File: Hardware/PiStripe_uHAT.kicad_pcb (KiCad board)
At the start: 2 copper layers, 65 x 30 mm, 43 parts, among them J1 +12V, J2 LED, J3 IRRX, J4 RPi_GPIO, Q1 DMG2305UX-13, Q2 IRF8721PBF-1, Q3 IRF8721PBF-1, Q4 IRF8721PBF-1, U1 TPS54202, U2 DMMT5401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

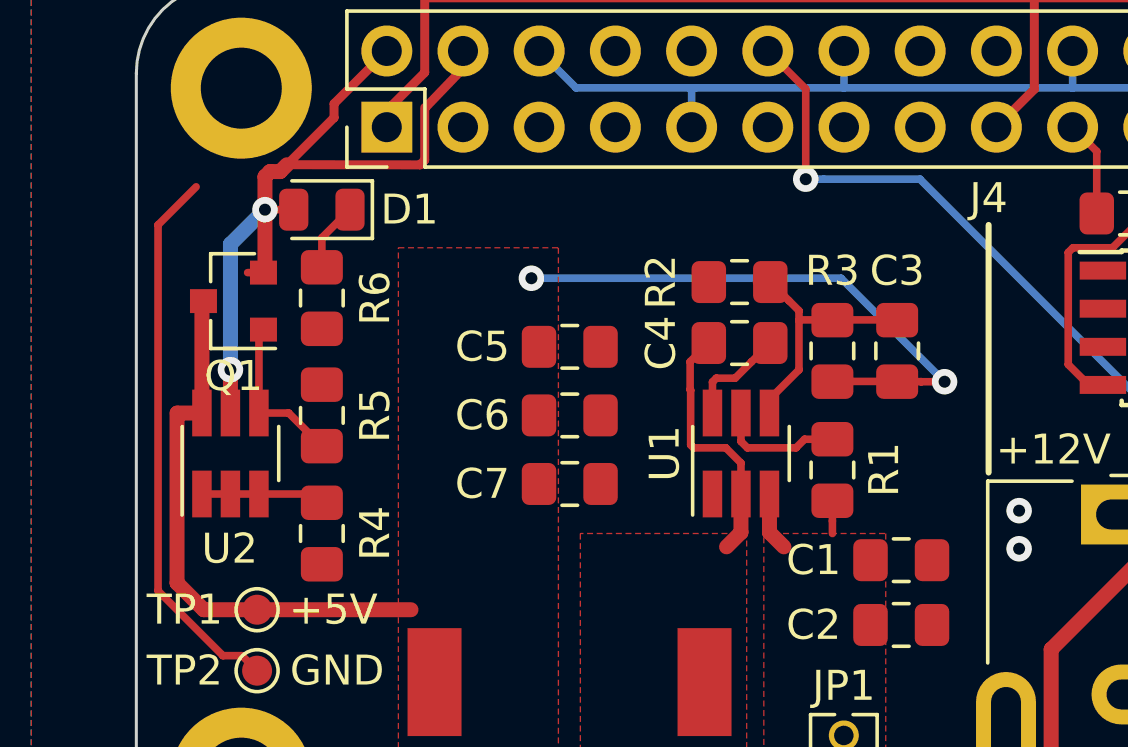
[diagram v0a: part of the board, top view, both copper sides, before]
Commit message: PCB: Add one more guide line, move C5-C7 a bit
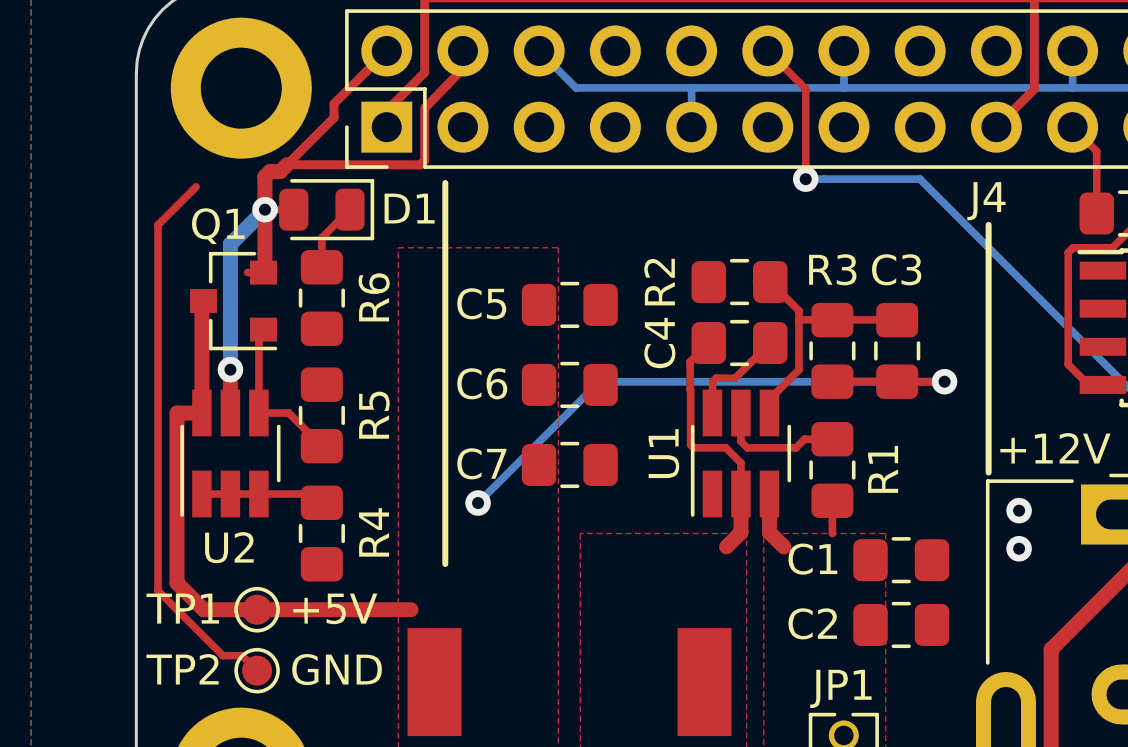
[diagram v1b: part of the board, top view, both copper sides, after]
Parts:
- moved C5 1.40 mm to (162.9, 85.7)
- moved C6 1.02 mm to (162.9, 88.4)
- moved C7 0.64 mm to (162.9, 91.1)
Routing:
- net Net-(C3-Pad2): track 36.8 -> 38.8 mm
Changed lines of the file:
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@@
   (general
     (thickness 1.6)
-    (drawings 21)
+    (drawings 22)
     (tracks 314)
     (zones 0)
@@
     (tags SOT-23)
     (attr smd)
-    (fp_text reference Q1 (at 0 -2.5 180) (layer F.SilkS)
+    (fp_text reference Q1 (at 0.4826 2.54 180) (layer F.SilkS)
       (effects (font (size 1 1) (thickness 0.15)))
     )
@@
   )
   (module Capacitor_SMD:C_0805_2012Metric_Pad1.15x1.40mm_HandSolder (layer F.Cu)
-    (at 162.95 87.122)
+    (at 162.95 85.725)
     (descr "Capacitor SMD 0805 (2012 Metric), square (rectangular) end terminal, IPC_7351 nominal with elongated pad for handsoldering. (Body size source: https://docs.google.com/spreadsheets/d/1BsfQQcO9C6DZCsRaXUlFlo91Tg2WpOkGARC1WS5S8t0/edit?usp=sharing), generated with kicad-footprint-generator")
     (tags "capacitor handsolder")
@@
   )
   (module Capacitor_SMD:C_0805_2012Metric_Pad1.15x1.40mm_HandSolder (layer F.Cu)
-    (at 162.95 89.408)
+    (at 162.95 88.392)
     (descr "Capacitor SMD 0805 (2012 Metric), square (rectangular) end terminal, IPC_7351 nominal with elongated pad for handsoldering. (Body size source: https://docs.google.com/spreadsheets/d/1BsfQQcO9C6DZCsRaXUlFlo91Tg2WpOkGARC1WS5S8t0/edit?usp=sharing), generated with kicad-footprint-generator")
     (tags "capacitor handsolder")
@@
   )
   (module Capacitor_SMD:C_0805_2012Metric_Pad1.15x1.40mm_HandSolder (layer F.Cu)
-    (at 162.95 91.694)
+    (at 162.95 91.059)
     (descr "Capacitor SMD 0805 (2012 Metric), square (rectangular) end terminal, IPC_7351 nominal with elongated pad for handsoldering. (Body size source: https://docs.google.com/spreadsheets/d/1BsfQQcO9C6DZCsRaXUlFlo91Tg2WpOkGARC1WS5S8t0/edit?usp=sharing), generated with kicad-footprint-generator")
     (tags "capacitor handsolder")
@@
     )
   )
+  (gr_line (start 158.8008 81.661) (end 158.8008 94.361) (layer F.SilkS) (width 0.2))
   (gr_line (start 176.911 91.313) (end 176.911 83.058) (layer F.SilkS) (width 0.2))
   (gr_line (start 202.184 97.409) (end 207.391 97.409) (layer F.SilkS) (width 0.2))
@@
   (segment (start 150.688 85.5996) (end 150.6896 85.598) (width 0.5) (layer F.Cu) (net 26))
   (segment (start 150.688 89.328) (end 150.688 85.5996) (width 0.5) (layer F.Cu) (net 26))
-  (via (at 161.671 84.836) (size 0.85) (drill 0.4) (layers F.Cu B.Cu) (net 26))
   (segment (start 152.908 95.885) (end 157.6578 95.885) (width 0.5) (layer F.Cu) (net 26))
   (segment (start 149.858999 89.332801) (end 149.858999 94.994999) (width 0.5) (layer F.Cu) (net 26))
@@
   (segment (start 175.44288 88.28532) (end 175.44288 88.28532) (width 0.254) (layer F.Cu) (net 26))
   (via (at 175.44288 88.28532) (size 0.85) (drill 0.4) (layers F.Cu B.Cu) (net 26))
-  (segment (start 171.99356 84.836) (end 175.44288 88.28532) (width 0.254) (layer B.Cu) (net 26))
-  (segment (start 161.671 84.836) (end 171.99356 84.836) (width 0.254) (layer B.Cu) (net 26))
+  (via (at 159.893 92.329) (size 0.85) (drill 0.4) (layers F.Cu B.Cu) (net 26))
+  (segment (start 163.93668 88.28532) (end 159.893 92.329) (width 0.254) (layer B.Cu) (net 26))
+  (segment (start 175.44288 88.28532) (end 163.93668 88.28532) (width 0.254) (layer B.Cu) (net 26))
   (segment (start 204.597 98.543) (end 204.597 99.292) (width 0.254) (layer F.Cu) (net 27))
   (segment (start 204.597 99.673) (end 204.597 99.051) (width 0.254) (layer F.Cu) (net 27))

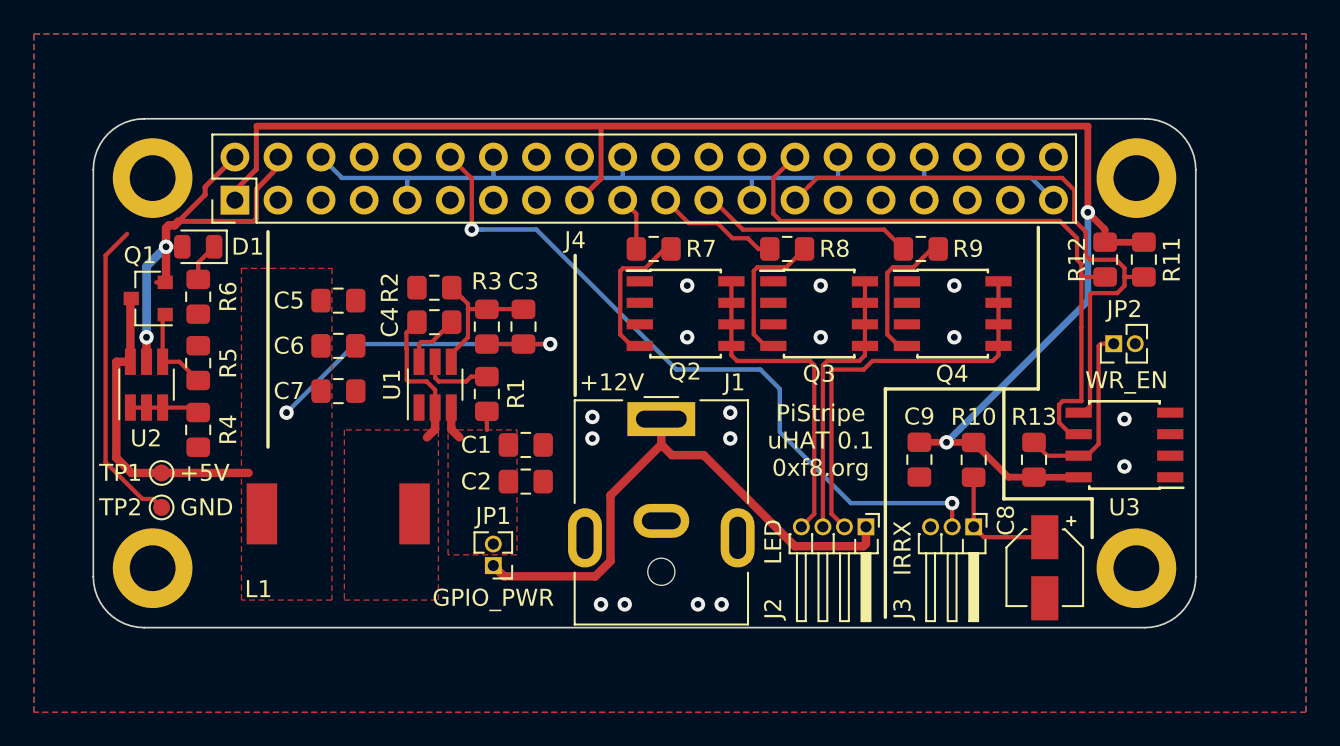
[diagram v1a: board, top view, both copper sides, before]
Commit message: v0.2: Small purely cosmetical update to the PCB
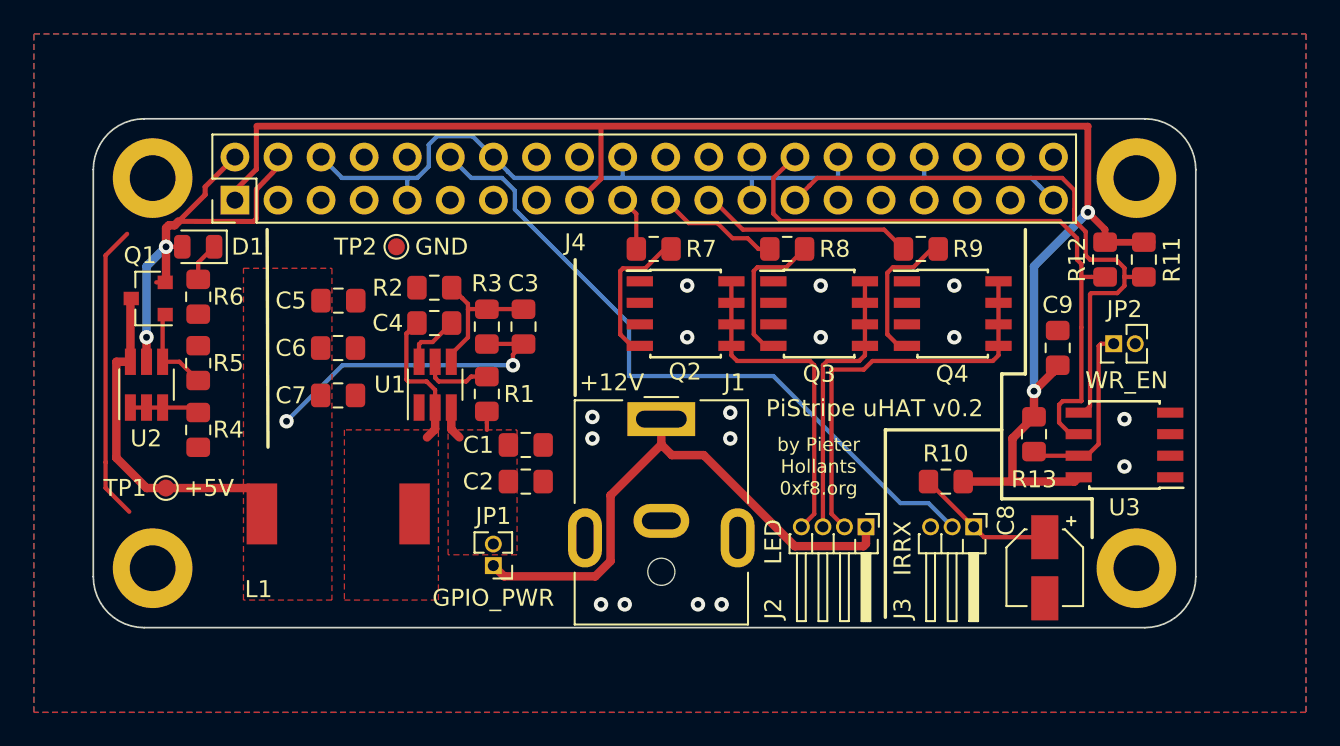
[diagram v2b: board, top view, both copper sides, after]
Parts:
- moved TP2 20.7 mm to (166.4, 82.5)
- moved C9 10.5 mm to (205.4, 88.5), turned to 270 degrees
- moved R10 2.08 mm to (198.8, 96.4), turned to 0 degrees
- moved R13 1.51 mm to (204.0, 93.6), turned to 270 degrees
- moved TP1 0.92 mm to (152.8, 96.8)
- moved C7 0.25 mm to (162.9, 91.3)
- moved C6 0.13 mm to (162.9, 88.5)
- moved C4 0.05 mm to (168.6, 87.0)
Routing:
- net Net-(C3-Pad2): track 38.8 -> 36.6 mm
- net Net-(J3-Pad2): track 42.8 -> 41.2 mm, vias 2 -> 0
- net Net-(C8-Pad1): track 8.74 -> 9.59 mm
- net GND: track 71.6 -> 72.3 mm
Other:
- board text added: "PiStripe uHAT v0.2"
- board text added: "by Pieter Hollants 0xf8.org"
- board text removed: "PiStripe uHAT 0.1 0xf8.org"

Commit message: v0.3: Additional Vias on GND plane near TPS54202, C9 routing optimized
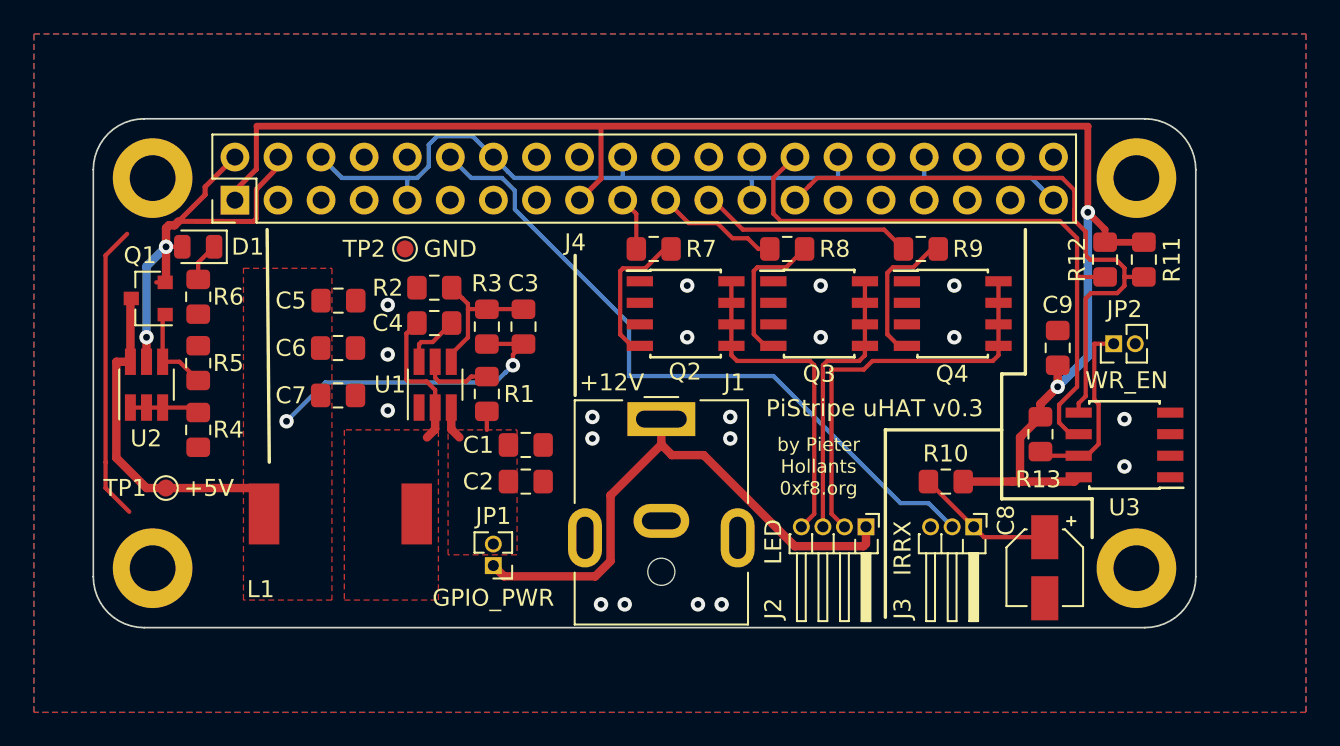
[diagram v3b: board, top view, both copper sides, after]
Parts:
- moved TP2 0.52 mm to (166.9, 82.7)
- moved R13 0.38 mm to (204.3, 93.6)
- moved L1 0.13 mm to (163.1, 98.3)
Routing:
- net +3V3: track 96.9 -> 95.6 mm
- net Net-(J4-Pad28): track 37.4 -> 36.8 mm
- net GND: vias 16 -> 19
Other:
- board text added: "PiStripe uHAT v0.3"
- board text removed: "PiStripe uHAT v0.2"

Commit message: v0.4: Change GPIO for IRRX from Pin 12 (GPIO18) to 22 (GPIO25)
Pin 12/GPIO18 is used by the phatDAC HAT which I want to combine with my
PiStripe uHAT.
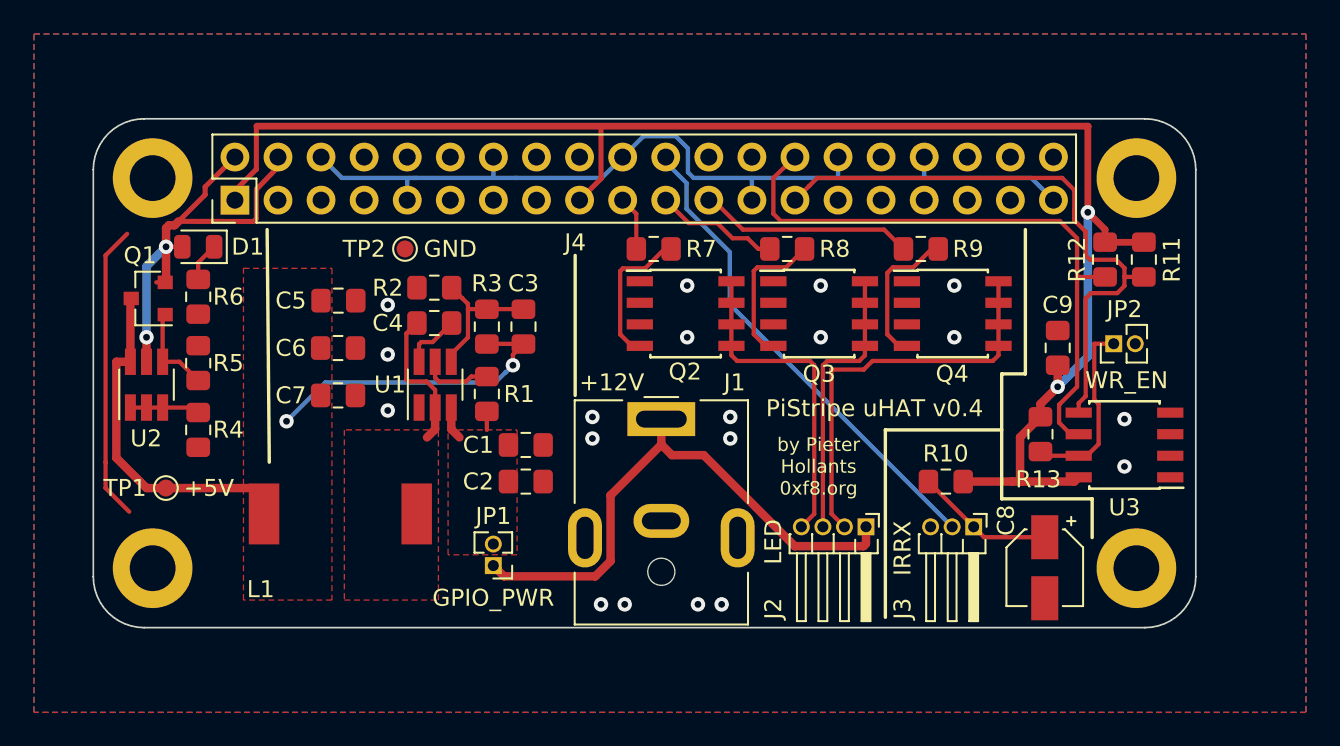
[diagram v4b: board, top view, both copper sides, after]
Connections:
- J4 pad 12: Net-(J3-Pad2) -> (no net)
- J4 pad 22: (no net) -> Net-(J3-Pad2)
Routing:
- net Net-(J3-Pad2): track 41.2 -> 28.8 mm
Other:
- board text added: "PiStripe uHAT v0.4"
- board text removed: "PiStripe uHAT v0.3"

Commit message: Board v0.5: Tidy right half of PCB
- Move Q2/Q3/Q4 more to the left
- Use generated space to move U3, R11, R12, R13 and C9 up right, placing
  JP2 below U3, making it visually easier to find
- Move C8 next to R10, above J3
- Connect to J1 separately from both sides to ensure better voltage flow
- Add pin description labels to J2 and J3 (note J2 R/G/B assignment may
  change again to match my actual LED stripe but these are assigned by
  software/choice of GPIO pins anyway)
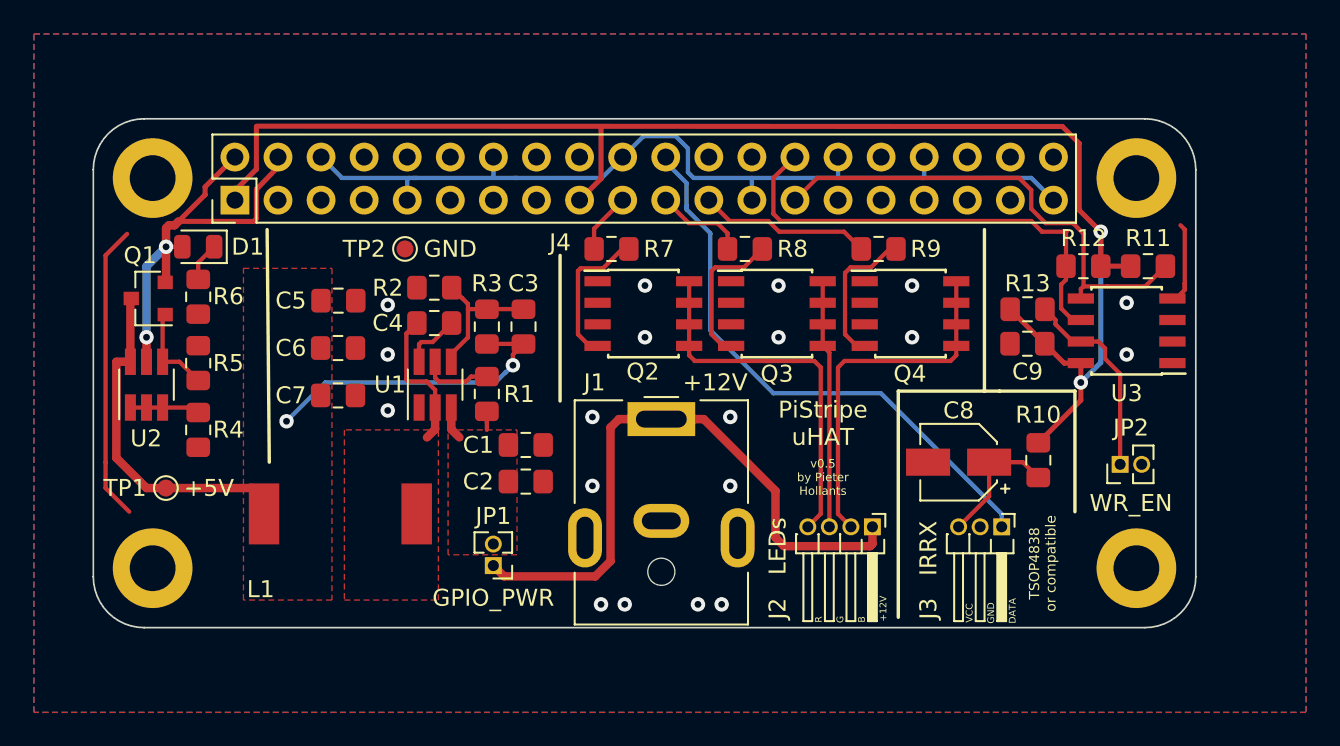
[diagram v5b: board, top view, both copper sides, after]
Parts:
- J2: value LED -> LEDs
- moved C8 8.03 mm to (199.5, 95.2), turned to 180 degrees
- moved R13 7.41 mm to (203.6, 86.2), turned to 0 degrees
- moved JP2 7.12 mm to (209.0, 95.4)
- moved U3 6.73 mm to (209.4, 87.5)
- moved R10 5.60 mm to (204.2, 95.1), turned to 90 degrees
- moved Q4 2.49 mm to (196.7, 86.5)
- moved Q2 2.49 mm to (180.9, 86.5)
- moved Q3 2.49 mm to (188.8, 86.5)
- moved R7 2.49 mm to (179.1, 82.7)
- moved R8 2.49 mm to (186.9, 82.7)
- moved R9 2.49 mm to (194.8, 82.7)
- moved C9 1.80 mm to (203.6, 88.3), turned to 0 degrees
- moved J3 1.65 mm to (202.1, 99.1)
- moved R12 1.34 mm to (206.9, 83.7), turned to 0 degrees
- moved R11 0.46 mm to (210.7, 83.7), turned to 180 degrees
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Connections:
- C1 pad 1: GND -> Net-(C1-Pad1)
- C1 pad 2: Net-(C1-Pad2) -> GND
- C2 pad 1: GND -> Net-(C1-Pad1)
- C2 pad 2: Net-(C1-Pad2) -> GND
- J3 pad 1: Net-(C8-Pad1) -> Net-(J3-Pad1)
- J3 pad 2: Net-(J3-Pad2) -> GND
- J3 pad 3: GND -> Net-(C8-Pad1)
- J4 pad 22: Net-(J3-Pad2) -> Net-(J3-Pad1)
- JP1 pad 2: Net-(C1-Pad2) -> Net-(C1-Pad1)
- R1 pad 1: Net-(C1-Pad2) -> Net-(C1-Pad1)
- R6 pad 1: GND -> Net-(D1-Pad1)
- R6 pad 2: Net-(D1-Pad1) -> GND
- U1 pad 3: Net-(C1-Pad2) -> Net-(C1-Pad1)
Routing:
- net Net-(J3-Pad1): track 0.00 -> 33.9 mm
- net Net-(J3-Pad2): track 28.8 -> 0.00 mm
- net Net-(J4-Pad28): track 36.8 -> 27.7 mm
- net Net-(J4-Pad27): track 36.4 -> 29.2 mm
- net +3V3: track 95.6 -> 90.1 mm
- net GND: track 72.7 -> 77.3 mm
- net Net-(J2-Pad4): track 19.3 -> 22.5 mm
- net +12V: track 34.8 -> 37.8 mm
- net Net-(C1-Pad2): track 3.05 -> 0.00 mm
- net Net-(C1-Pad1): track 0.00 -> 3.05 mm
- net Net-(J2-Pad2): track 24.1 -> 21.3 mm
- net Net-(J4-Pad23): track 12.7 -> 10.4 mm
- net Net-(J2-Pad3): track 16.6 -> 14.6 mm
- net Net-(J4-Pad21): track 7.33 -> 5.38 mm
- net Net-(C8-Pad1): track 9.59 -> 8.33 mm
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- added copper zone on F.Cu, net Net-(C1-Pad1)
- removed copper zone on F.Cu, net Net-(C1-Pad2)
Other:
- board text added: "+12V"
- board text added: "B"
- board text added: "DATA"
- board text added: "G"
- board text added: "GND"
- board text added: "PiStripe uHAT"
- board text added: "R"
- board text added: "TSOP4838 or compatible"
- board text added: "VCC"
- board text added: "v0.5 by Pieter Hollants"
- board text removed: "PiStripe uHAT v0.4"
- board text removed: "by Pieter Hollants 0xf8.org"
